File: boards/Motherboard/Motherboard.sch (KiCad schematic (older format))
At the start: 0 parts

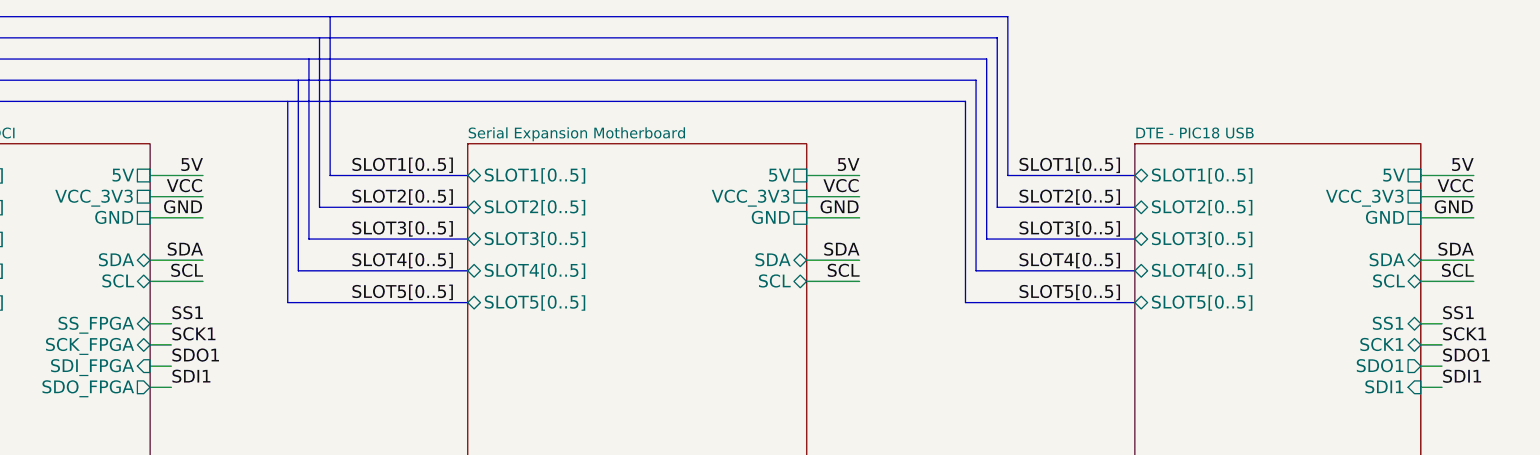
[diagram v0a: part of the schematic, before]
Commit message: Placed power ports on top sheet of motherboard. Fixes #21
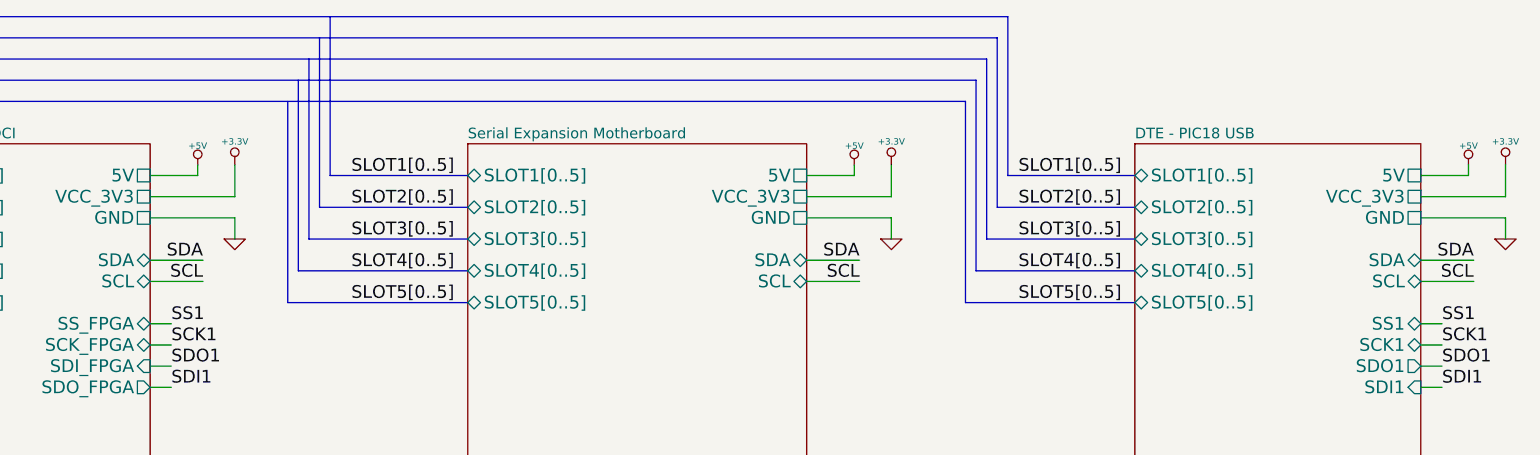
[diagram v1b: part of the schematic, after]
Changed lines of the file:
@@
 Text Label 7000 2400 2    60   ~ 0
 SCL
-Text Label 7000 1900 2    60   ~ 0
-5V
-Text Label 7000 2000 2    60   ~ 0
-VCC
-Text Label 7000 2100 2    60   ~ 0
-GND
-Text Label 3900 1900 2    60   ~ 0
-5V
-Text Label 3900 2000 2    60   ~ 0
-VCC
-Text Label 3900 2100 2    60   ~ 0
-GND
 Text Label 3900 2300 2    60   ~ 0
 SDA
@@
 Text Label 9900 2400 2    60   ~ 0
 SCL
-Text Label 9900 1900 2    60   ~ 0
-5V
-Text Label 9900 2000 2    60   ~ 0
-VCC
-Text Label 9900 2100 2    60   ~ 0
-GND
-Wire Wire Line
-	6750 1900 7000 1900
-Wire Wire Line
-	6750 2000 7000 2000
-Wire Wire Line
-	6750 2100 7000 2100
 Wire Wire Line
 	6750 2300 7000 2300
@@
 	6750 2400 7000 2400
 Wire Wire Line
-	3650 1900 3900 1900
-Wire Wire Line
-	3650 2000 3900 2000
-Wire Wire Line
-	3650 2100 3900 2100
+	3650 1900 3875 1900
+Wire Wire Line
+	3650 2000 4050 2000
+Wire Wire Line
+	3650 2100 4050 2100
 Wire Wire Line
 	3650 2300 3900 2300
@@
 Wire Wire Line
 	9650 2400 9900 2400
-Wire Wire Line
-	9650 1900 9900 1900
-Wire Wire Line
-	9650 2000 9900 2000
-Wire Wire Line
-	9650 2100 9900 2100
 Wire Wire Line
 	3650 2600 3750 2600
@@
 F15 "SLOT5[0..5]" T L 8300 2500 60
 $EndSheet
+$Comp
+L +5V #PWR?
+U 1 1 53B3A013
+P 3875 1850
+F 0 "#PWR?" H 3875 1940 20  0001 C CNN
+F 1 "+5V" H 3875 1940 30  0000 C CNN
+F 2 "" H 3875 1850 60  0000 C CNN
+F 3 "" H 3875 1850 60  0000 C CNN
+	1    3875 1850
+	1    0    0    -1
+$EndComp
+Wire Wire Line
+	3875 1900 3875 1850
+$Comp
+L +3.3V #PWR?
+U 1 1 53B3A1F1
+P 4050 1850
+F 0 "#PWR?" H 4050 1810 30  0001 C CNN
+F 1 "+3.3V" H 4050 1960 30  0000 C CNN
+F 2 "" H 4050 1850 60  0000 C CNN
+F 3 "" H 4050 1850 60  0000 C CNN
+	1    4050 1850
+	1    0    0    -1
+$EndComp
+Wire Wire Line
+	4050 2000 4050 1850
+$Comp
+L GND #PWR?
+U 1 1 53B3A928
+P 4050 2200
+F 0 "#PWR?" H 4050 2200 30  0001 C CNN
+F 1 "GND" H 4050 2130 30  0001 C CNN
+F 2 "" H 4050 2200 60  0000 C CNN
+F 3 "" H 4050 2200 60  0000 C CNN
+	1    4050 2200
+	1    0    0    -1
+$EndComp
+Wire Wire Line
+	4050 2100 4050 2200
+Wire Wire Line
+	6750 1900 6975 1900
+Wire Wire Line
+	6750 2000 7150 2000
+Wire Wire Line
+	6750 2100 7150 2100
+$Comp
+L +5V #PWR?
+U 1 1 53B3AD77
+P 6975 1850
+F 0 "#PWR?" H 6975 1940 20  0001 C CNN
+F 1 "+5V" H 6975 1940 30  0000 C CNN
+F 2 "" H 6975 1850 60  0000 C CNN
+F 3 "" H 6975 1850 60  0000 C CNN
+	1    6975 1850
+	1    0    0    -1
+$EndComp
+Wire Wire Line
+	6975 1900 6975 1850
+$Comp
+L +3.3V #PWR?
+U 1 1 53B3AD7E
+P 7150 1850
+F 0 "#PWR?" H 7150 1810 30  0001 C CNN
+F 1 "+3.3V" H 7150 1960 30  0000 C CNN
+F 2 "" H 7150 1850 60  0000 C CNN
+F 3 "" H 7150 1850 60  0000 C CNN
+	1    7150 1850
+	1    0    0    -1
+$EndComp
+Wire Wire Line
+	7150 2000 7150 1850
+$Comp
+L GND #PWR?
+U 1 1 53B3AD85
+P 7150 2200
+F 0 "#PWR?" H 7150 2200 30  0001 C CNN
+F 1 "GND" H 7150 2130 30  0001 C CNN
+F 2 "" H 7150 2200 60  0000 C CNN
+F 3 "" H 7150 2200 60  0000 C CNN
+	1    7150 2200
+	1    0    0    -1
+$EndComp
+Wire Wire Line
+	7150 2100 7150 2200
+Wire Wire Line
+	9650 1900 9875 1900
+Wire Wire Line
+	9650 2000 10050 2000
+Wire Wire Line
+	9650 2100 10050 2100
+$Comp
+L +5V #PWR?
+U 1 1 53B3B095
+P 9875 1850
+F 0 "#PWR?" H 9875 1940 20  0001 C CNN
+F 1 "+5V" H 9875 1940 30  0000 C CNN
+F 2 "" H 9875 1850 60  0000 C CNN
+F 3 "" H 9875 1850 60  0000 C CNN
+	1    9875 1850
+	1    0    0    -1
+$EndComp
+Wire Wire Line
+	9875 1900 9875 1850
+$Comp
+L +3.3V #PWR?
+U 1 1 53B3B09C
+P 10050 1850
+F 0 "#PWR?" H 10050 1810 30  0001 C CNN
+F 1 "+3.3V" H 10050 1960 30  0000 C CNN
+F 2 "" H 10050 1850 60  0000 C CNN
+F 3 "" H 10050 1850 60  0000 C CNN
+	1    10050 1850
+	1    0    0    -1
+$EndComp
+Wire Wire Line
+	10050 2000 10050 1850
+$Comp
+L GND #PWR?
+U 1 1 53B3B0A3
+P 10050 2200
+F 0 "#PWR?" H 10050 2200 30  0001 C CNN
+F 1 "GND" H 10050 2130 30  0001 C CNN
+F 2 "" H 10050 2200 60  0000 C CNN
+F 3 "" H 10050 2200 60  0000 C CNN
+	1    10050 2200
+	1    0    0    -1
+$EndComp
+Wire Wire Line
+	10050 2100 10050 2200
 $EndSCHEMATC

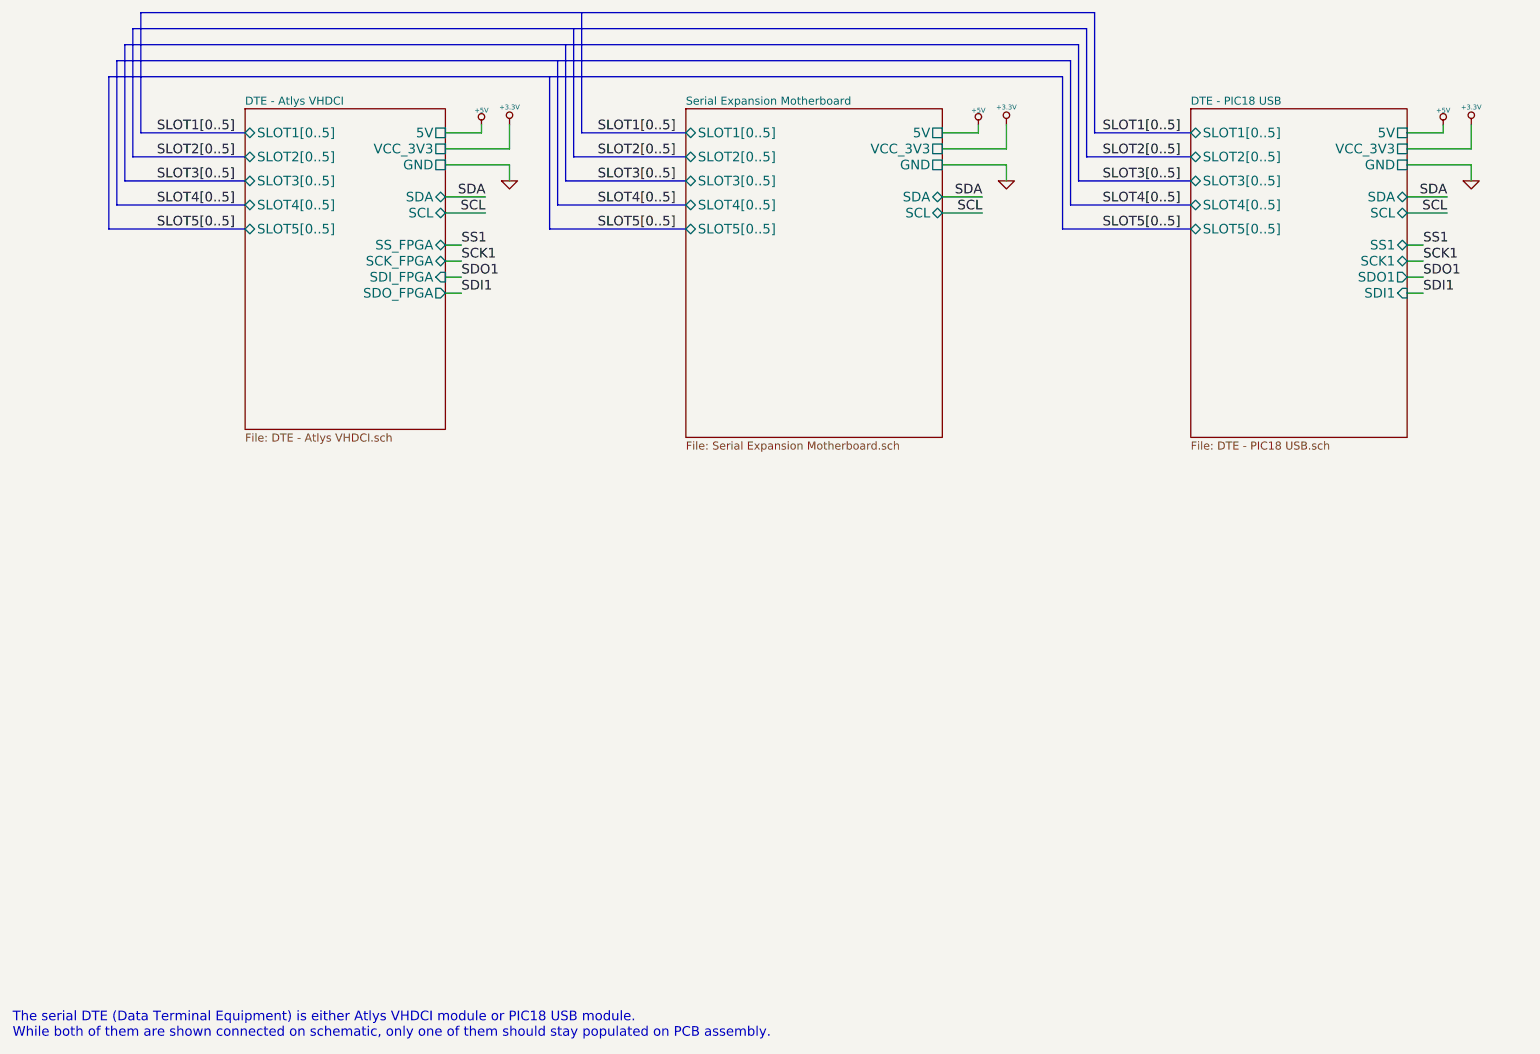
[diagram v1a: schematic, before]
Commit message: Connected SPI and I2C with wires in mboard top sheet
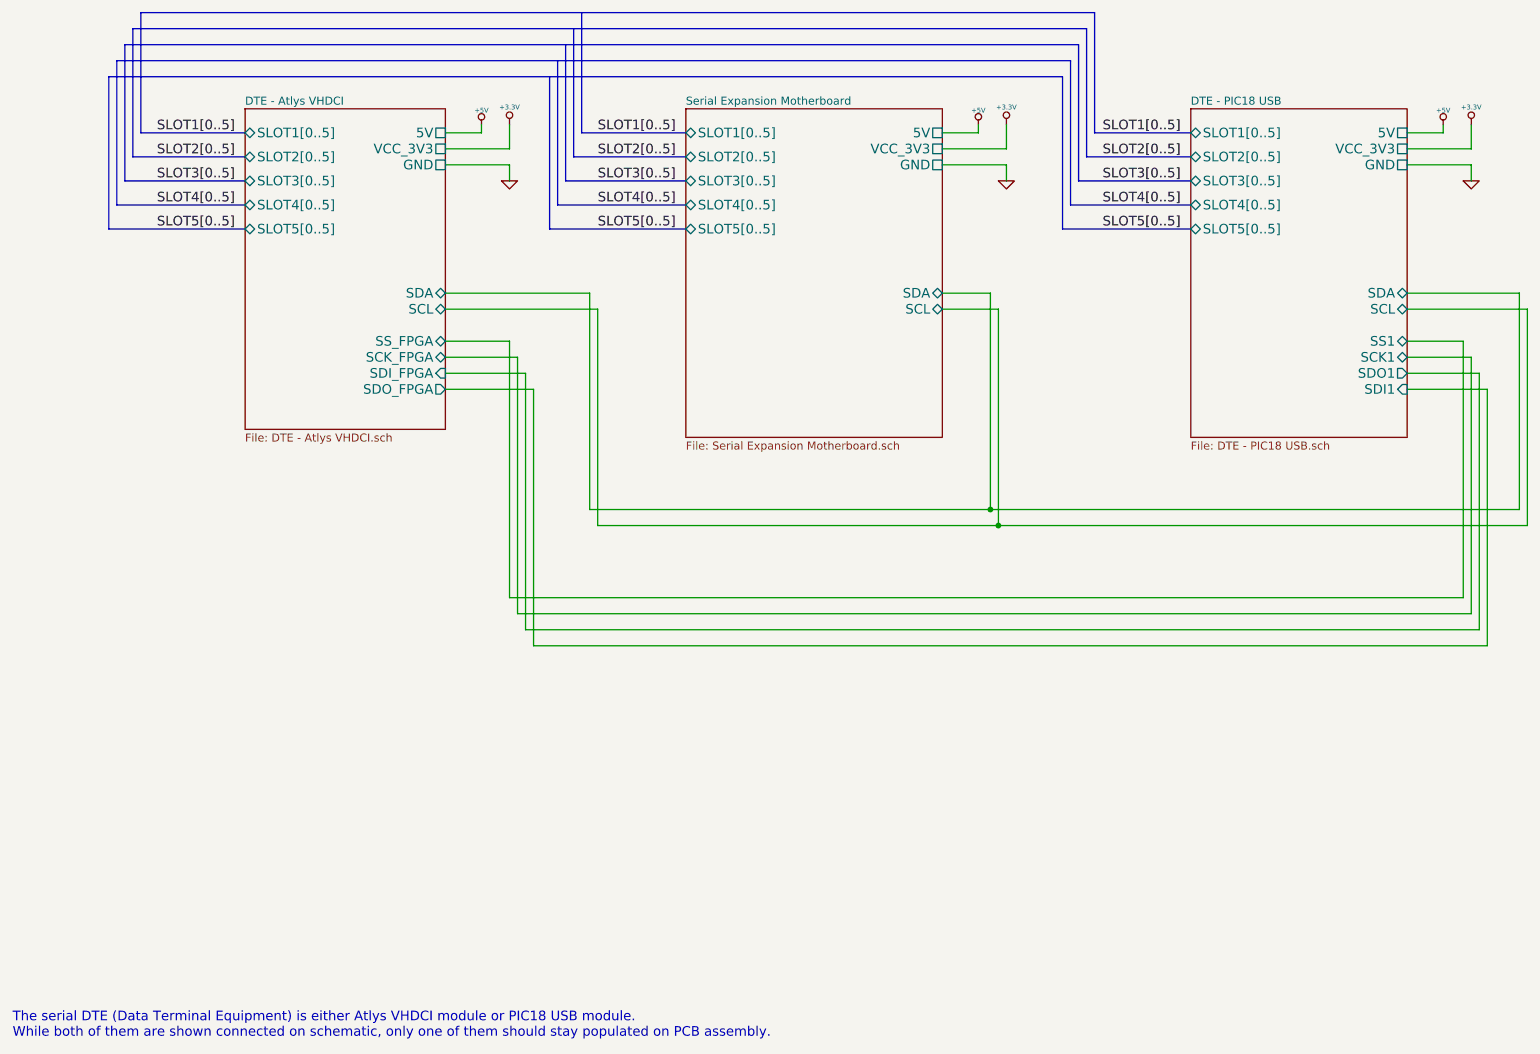
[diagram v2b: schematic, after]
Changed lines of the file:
@@
 Text Notes 950  7550 0    60   ~ 0
 The serial DTE (Data Terminal Equipment) is either Atlys VHDCI module or PIC18 USB module.\nWhile both of them are shown connected on schematic, only one of them should stay populated on PCB assembly.
-Text Label 7000 2300 2    60   ~ 0
-SDA
-Text Label 7000 2400 2    60   ~ 0
-SCL
-Text Label 3900 2300 2    60   ~ 0
-SDA
-Text Label 3900 2400 2    60   ~ 0
-SCL
-Text Label 9900 2300 2    60   ~ 0
-SDA
-Text Label 9900 2400 2    60   ~ 0
-SCL
-Wire Wire Line
-	6750 2300 7000 2300
-Wire Wire Line
-	6750 2400 7000 2400
+Wire Wire Line
+	6750 2900 7050 2900
+Wire Wire Line
+	6750 3000 7100 3000
 Wire Wire Line
 	3650 1900 3875 1900
@@
 	3650 2100 4050 2100
 Wire Wire Line
-	3650 2300 3900 2300
-Wire Wire Line
-	3650 2400 3900 2400
-Wire Wire Line
-	9650 2300 9900 2300
-Wire Wire Line
-	9650 2400 9900 2400
-Wire Wire Line
-	3650 2600 3750 2600
-Wire Wire Line
-	3650 2700 3750 2700
-Wire Wire Line
-	3650 2800 3750 2800
-Wire Wire Line
-	3650 2900 3750 2900
-Wire Wire Line
-	9650 2600 9750 2600
-Wire Wire Line
-	9650 2700 9750 2700
-Wire Wire Line
-	9650 2800 9750 2800
-Wire Wire Line
-	9650 2900 9750 2900
-Text Label 3750 2600 0    60   ~ 0
-SS1
-Text Label 3750 2700 0    60   ~ 0
-SCK1
-Text Label 3750 2800 0    60   ~ 0
-SDO1
-Text Label 3750 2900 0    60   ~ 0
-SDI1
-Text Label 9750 2600 0    60   ~ 0
-SS1
-Text Label 9750 2700 0    60   ~ 0
-SCK1
-Text Label 9750 2800 0    60   ~ 0
-SDO1
-Text Label 9750 2900 0    60   ~ 0
-SDI1
+	3650 2900 4550 2900
+Wire Wire Line
+	3650 3000 4600 3000
+Wire Wire Line
+	9650 2900 10350 2900
+Wire Wire Line
+	9650 3000 10400 3000
+Wire Wire Line
+	3650 3200 4050 3200
+Wire Wire Line
+	3650 3300 4100 3300
+Wire Wire Line
+	3650 3400 4150 3400
+Wire Wire Line
+	3650 3500 4200 3500
+Wire Wire Line
+	9650 3200 10000 3200
+Wire Wire Line
+	9650 3300 10050 3300
+Wire Wire Line
+	9650 3400 10100 3400
+Wire Wire Line
+	9650 3500 10150 3500
 $Sheet
 S 2400 1750 1250 2000
@@
 F3 "5V" U R 3650 1900 60
 F4 "VCC_3V3" U R 3650 2000 60
-F5 "SDA" B R 3650 2300 60
-F6 "SCL" B R 3650 2400 60
-F7 "SS_FPGA" T R 3650 2600 60
-F8 "SCK_FPGA" T R 3650 2700 60
-F9 "SDI_FPGA" I R 3650 2800 60
-F10 "SDO_FPGA" O R 3650 2900 60
+F5 "SDA" B R 3650 2900 60
+F6 "SCL" B R 3650 3000 60
+F7 "SS_FPGA" T R 3650 3200 60
+F8 "SCK_FPGA" T R 3650 3300 60
+F9 "SDI_FPGA" I R 3650 3400 60
+F10 "SDO_FPGA" O R 3650 3500 60
 F11 "SLOT1[0..5]" T L 2400 1900 60
 F12 "SLOT2[0..5]" T L 2400 2050 60
@@
 F3 "VCC_3V3" U R 6750 2000 60
 F4 "GND" U R 6750 2100 60
-F5 "SDA" B R 6750 2300 60
-F6 "SCL" B R 6750 2400 60
+F5 "SDA" B R 6750 2900 60
+F6 "SCL" B R 6750 3000 60
 F7 "SLOT1[0..5]" B L 5150 1900 60
 F8 "SLOT2[0..5]" B L 5150 2050 60
@@
 F3 "GND" U R 9650 2100 60
 F4 "VCC_3V3" U R 9650 2000 60
-F5 "SDA" B R 9650 2300 60
-F6 "SCL" B R 9650 2400 60
-F7 "SS1" T R 9650 2600 60
-F8 "SCK1" T R 9650 2700 60
-F9 "SDI1" I R 9650 2900 60
-F10 "SDO1" O R 9650 2800 60
+F5 "SDA" B R 9650 2900 60
+F6 "SCL" B R 9650 3000 60
+F7 "SS1" T R 9650 3200 60
+F8 "SCK1" T R 9650 3300 60
+F9 "SDI1" I R 9650 3500 60
+F10 "SDO1" O R 9650 3400 60
 F11 "SLOT1[0..5]" T L 8300 1900 60
 F12 "SLOT2[0..5]" T L 8300 2050 60
@@
 Wire Wire Line
 	10050 2100 10050 2200
+Wire Wire Line
+	4600 3000 4600 4350
+Wire Wire Line
+	4600 4350 10400 4350
+Wire Wire Line
+	10400 4350 10400 3000
+Wire Wire Line
+	4550 2900 4550 4250
+Wire Wire Line
+	4550 4250 10350 4250
+Wire Wire Line
+	10350 4250 10350 2900
+Wire Wire Line
+	7050 2900 7050 4250
+Connection ~ 7050 4250
+Wire Wire Line
+	7100 3000 7100 4350
+Connection ~ 7100 4350
+Wire Wire Line
+	4050 3200 4050 4800
+Wire Wire Line
+	4050 4800 10000 4800
+Wire Wire Line
+	10000 4800 10000 3200
+Wire Wire Line
+	4100 3300 4100 4900
+Wire Wire Line
+	4100 4900 10050 4900
+Wire Wire Line
+	10050 4900 10050 3300
+Wire Wire Line
+	4150 3400 4150 5000
+Wire Wire Line
+	4150 5000 10100 5000
+Wire Wire Line
+	10100 5000 10100 3400
+Wire Wire Line
+	4200 3500 4200 5100
+Wire Wire Line
+	4200 5100 10150 5100
+Wire Wire Line
+	10150 5100 10150 3500
 $EndSCHEMATC

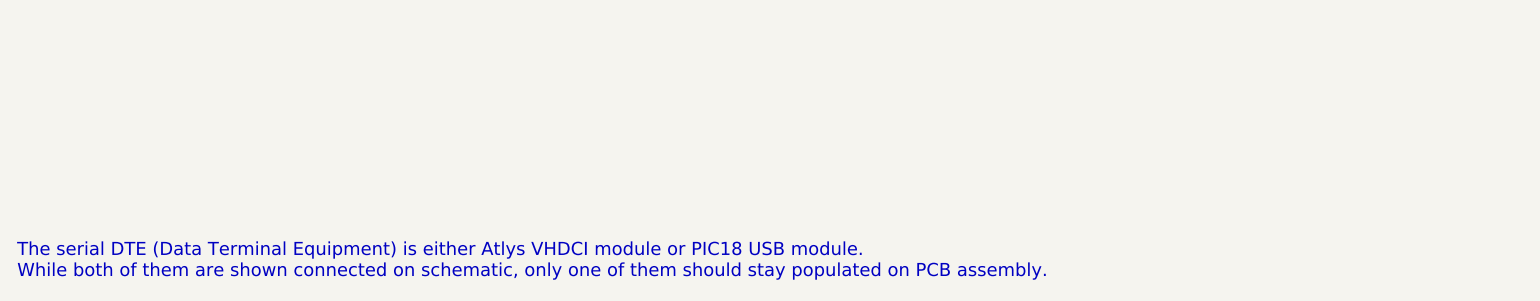
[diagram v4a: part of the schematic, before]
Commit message: Updated motherboard schematic to use new dboard_slot component
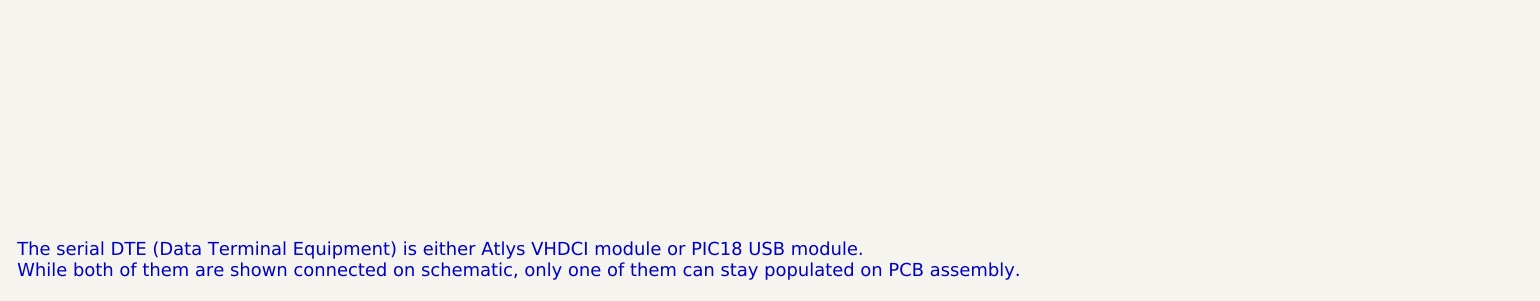
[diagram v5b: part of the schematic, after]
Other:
- note added: "The serial DTE (Data Terminal Equipment) is either Atlys VHDCI module or PIC18 USB module.\nWhile both of them are shown connected on schematic, only one of them can stay populated on PCB assembly."
- note removed: "The serial DTE (Data Terminal Equipment) is either Atlys VHDCI module or PIC18 USB module.\nWhile both of them are shown connected on schematic, only one of them should stay populated on PCB assembly."
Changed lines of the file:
@@
 LIBS:CONN_16
 LIBS:csmall
+LIBS:dboard_slot
 LIBS:Motherboard-cache
 EELAYER 27 0
@@
 Sheet 1 7
 Title "Serial Expansion Module and DTE interface"
-Date "4 jul 2014"
+Date "5 jul 2014"
 Rev ""
 Comp "TimVideos"
@@
 $EndDescr
 Text Notes 950  7550 0    60   ~ 0
-The serial DTE (Data Terminal Equipment) is either Atlys VHDCI module or PIC18 USB module.\nWhile both of them are shown connected on schematic, only one of them should stay populated on PCB assembly.
+The serial DTE (Data Terminal Equipment) is either Atlys VHDCI module or PIC18 USB module.\nWhile both of them are shown connected on schematic, only one of them can stay populated on PCB assembly.
 Wire Wire Line
 	6750 2900 7050 2900
